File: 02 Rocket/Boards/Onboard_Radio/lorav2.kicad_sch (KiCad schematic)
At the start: 31 parts, among them J6 RFIO SMA, U2 SX1262, U3 PE4259 RF Switch, Y1 32.000MHz

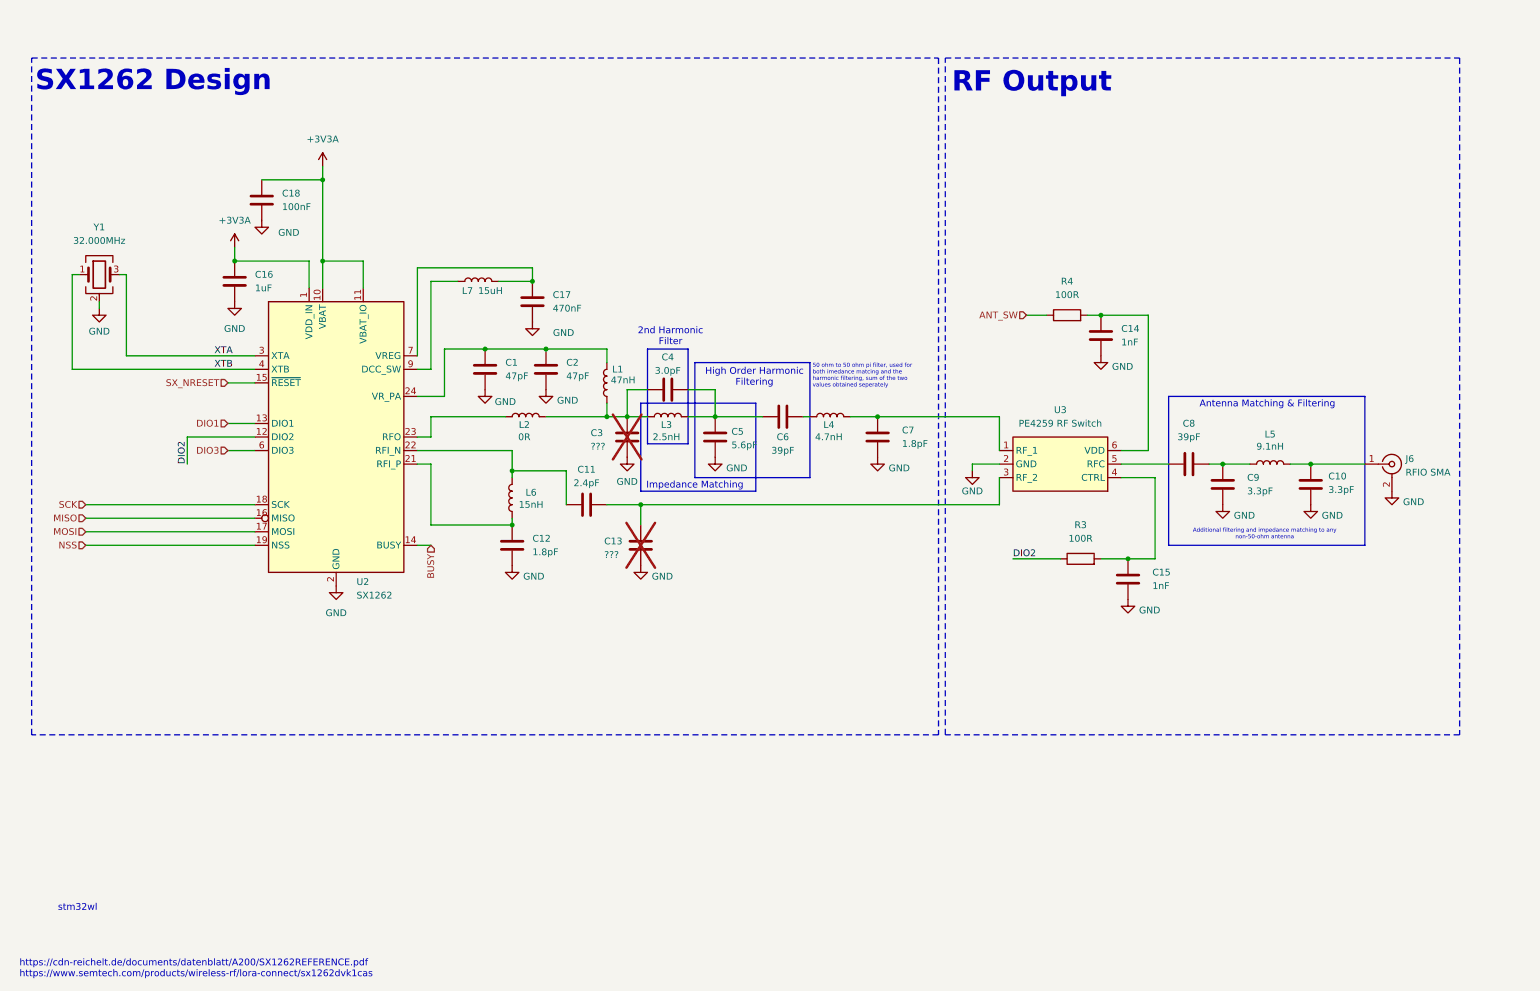
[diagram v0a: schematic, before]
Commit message: updates to schematic notes
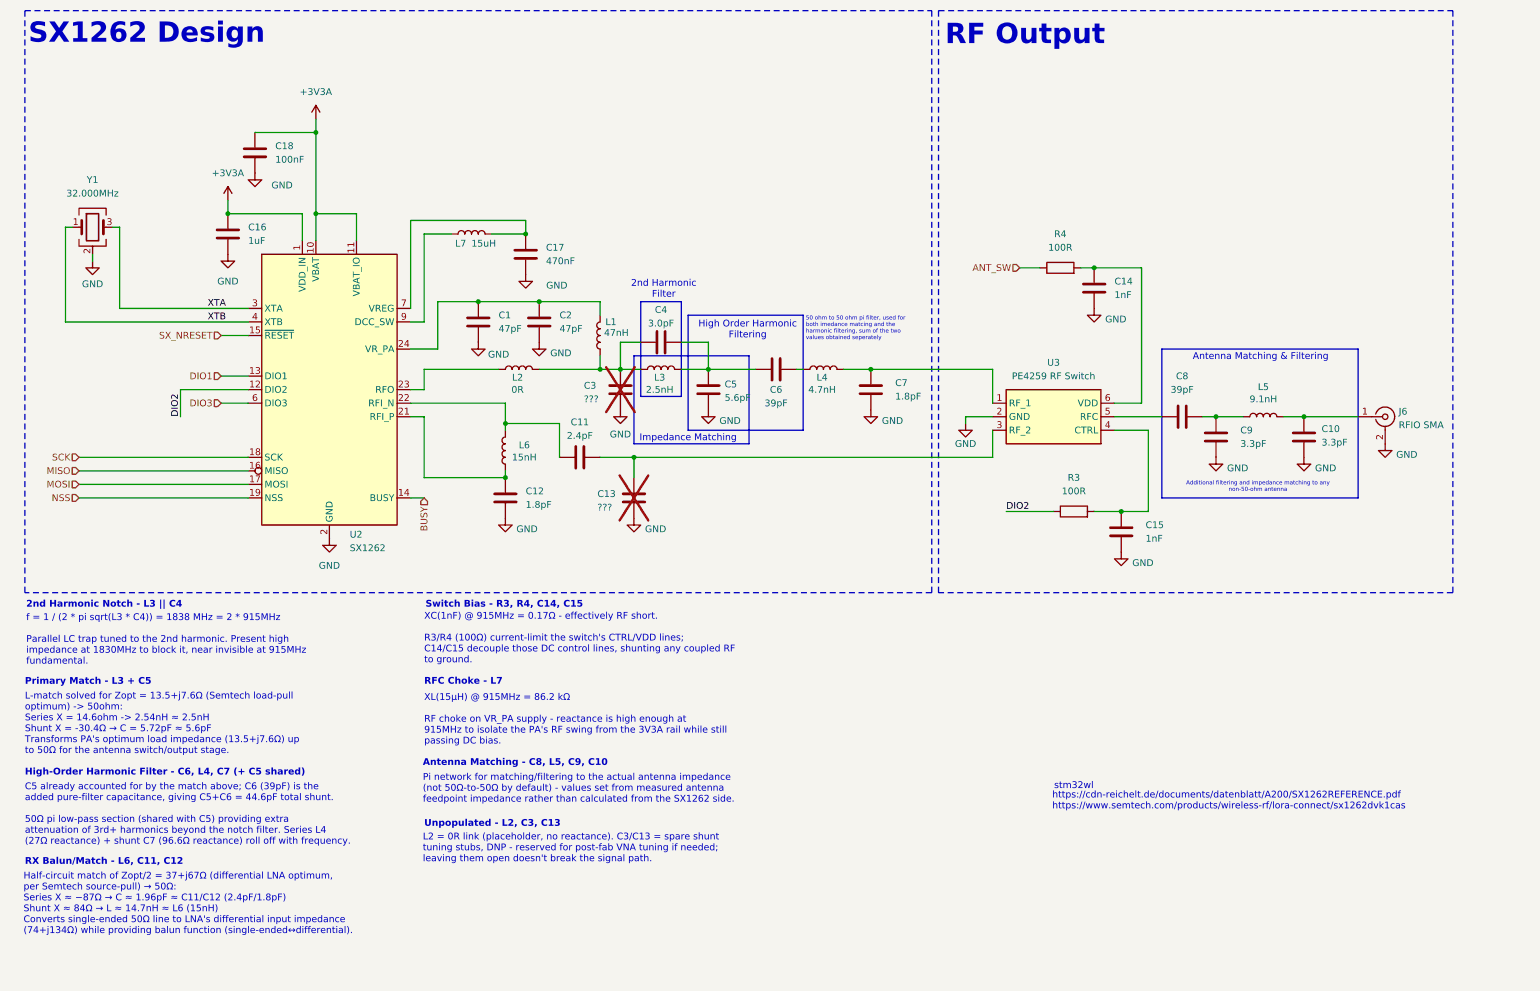
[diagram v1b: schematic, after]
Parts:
- U3: MPN PE4259 -> 4259-63
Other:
- note added: "2nd Harmonic Notch - L3 || C4"
- note added: "Antenna Matching - C8, L5, C9, C10"
- note added: "C5 already accounted for by the match above; C6 (39pF) is the added pure-filter capacitance, giving C5+C6 = 44.6pF total shunt. 50Ω pi low-pass section (shared with C5) providing extra attenuation of 3rd+ harmonics beyond the notch filter. Series L4 (27Ω reactance) + shunt C7 (96.6Ω reactance) roll off with frequency."
- note added: "Half-circuit match of Zopt/2 = 37+j67Ω (differential LNA optimum, per Semtech source-pull) → 50Ω: Series X ≈ −87Ω → C ≈ 1.96pF ≈ C11/C12 (2.4pF/1.8pF) Shunt X ≈ 84Ω → L ≈ 14.7nH ≈ L6 (15nH) Converts single-ended 50Ω line to LNA's differential input impedance (74+j134Ω) while providing balun function (single-ended↔differential)."
- note added: "High-Order Harmonic Filter - C6, L4, C7 (+ C5 shared)"
- note added: "L-match solved for Zopt = 13.5+j7.6Ω (Semtech load-pull optimum) -> 50ohm: Series X = 14.6ohm -> 2.54nH ≈ 2.5nH Shunt X = -30.4Ω → C = 5.72pF ≈ 5.6pF Transforms PA's optimum load impedance (13.5+j7.6Ω) up to 50Ω for the antenna switch/output stage."
- note added: "L2 = 0R link (placeholder, no reactance). C3/C13 = spare shunt tuning stubs, DNP - reserved for post-fab VNA tuning if needed; leaving them open doesn't break the signal path."
- note added: "Pi network for matching/filtering to the actual antenna impedance (not 50Ω-to-50Ω by default) - values set from measured antenna feedpoint impedance rather than calculated from the SX1262 side."
- note added: "Primary Match - L3 + C5"
- note added: "RFC Choke - L7"
- note added: "RX Balun/Match - L6, C11, C12"
- note added: "Switch Bias - R3, R4, C14, C15"
- note added: "Unpopulated - L2, C3, C13"
- note added: "XC(1nF) @ 915MHz = 0.17Ω - effectively RF short. R3/R4 (100Ω) current-limit the switch's CTRL/VDD lines; C14/C15 decouple those DC control lines, shunting any coupled RF to ground."
- note added: "XL(15µH) @ 915MHz = 86.2 kΩ RF choke on VR_PA supply - reactance is high enough at 915MHz to isolate the PA's RF swing from the 3V3A rail while still passing DC bias."
- note added: "f = 1 / (2 * pi sqrt(L3 * C4)) = 1838 MHz = 2 * 915MHz Parallel LC trap tuned to the 2nd harmonic. Present high impedance at 1830MHz to block it, near invisible at 915MHz fundamental."
- moved on the sheet: C1, C10, C11, C12, C13, C14, C15, C16, C17, C18, C2, C3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
